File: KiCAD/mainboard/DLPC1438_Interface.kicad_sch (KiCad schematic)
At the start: 92 parts, among them IC14 SN74AUP1G06DCKR, IC6 SN74AUP1G06DCKR, J10 Conn_01x05_Pin, J2 Conn_01x07_Pin, J29 Conn_01x04_Pin, J3 Conn_02x05_Odd_Even, J31 Conn_01x08_Pin, J4 Conn_01x05_Pin, U12 ECS-2520MV-xxx-xx, U13 MX25L3233FM2, U16 DLPC1438ZEZ, U22 TXS0102DCU, U37 TXS0102DCU, U7 SN74AUP1G06DCKR

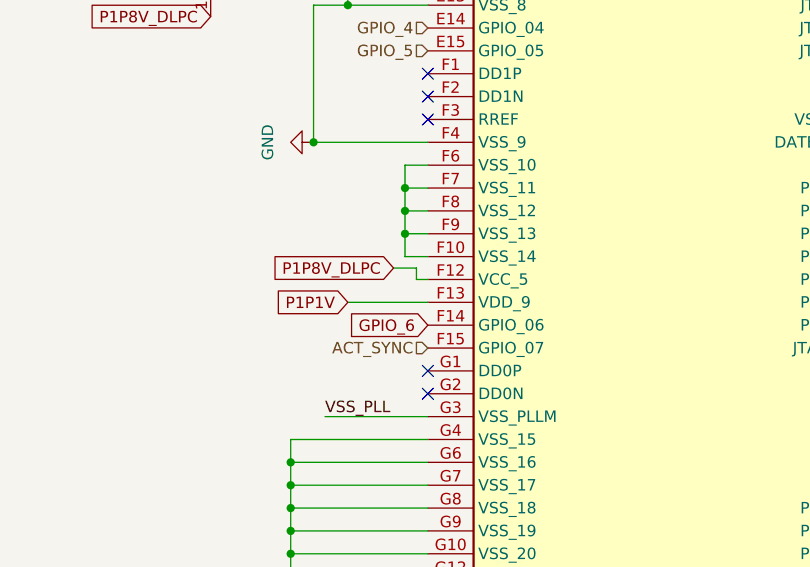
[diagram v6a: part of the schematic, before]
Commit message: layout, was able to fanout all not power signals without vias inside BGA, will only need normal vias size 0.3mm diameter for GND and power planes, plan is to have DMD signals on their own layer
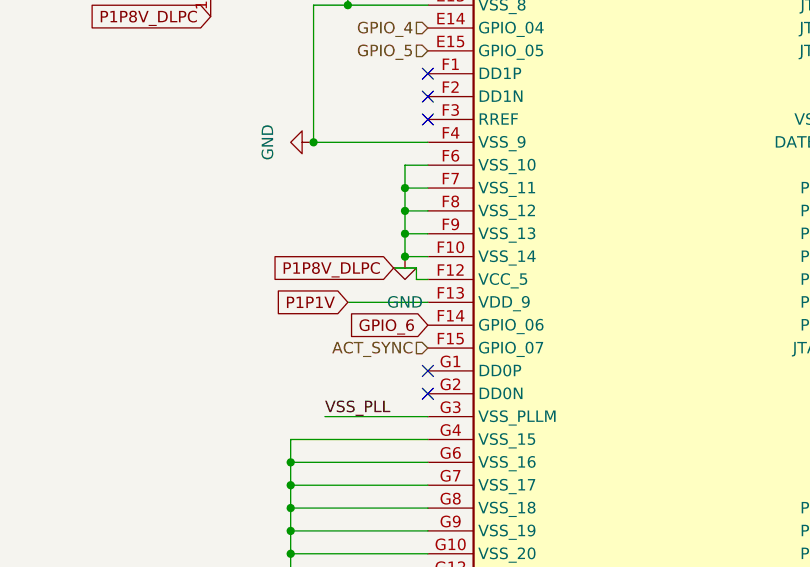
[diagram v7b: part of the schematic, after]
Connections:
- net GND: now also U16.F10 (VSS_14), U16.F6 (VSS_10), U16.F7 (VSS_11), U16.F8 (VSS_12), U16.F9 (VSS_13)
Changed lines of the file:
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@@
 	)
 	(junction
+		(at 359.41 237.49)
+		(diameter 0)
+		(color 0 0 0 0)
+	)
+	(junction
 		(at 251.46 66.04)
 		(diameter 0)
@@
 					(unit 1)
 				)
+			)
+		)
+	)
+	(symbol
+		(lib_id "power:GND")
+		(at 359.41 237.49 0)
+		(unit 1)
+		(exclude_from_sim no)
+		(in_bom yes)
+		(on_board yes)
+		(dnp no)
+		(fields_autoplaced yes)
+		(property "Reference" "#PWR066"
+			(at 359.41 243.84 0)
+			(effects
+				(font
+					(size 1.27 1.27)
+				)
+				(hide yes)
+			)
+		)
+		(property "Value" "GND"
+			(at 359.41 242.57 0)
+			(effects
+				(font
+					(size 1.27 1.27)
+				)
+			)
+		)
+		(property "Footprint" ""
+			(at 359.41 237.49 0)
+			(effects
+				(font
+					(size 1.27 1.27)
+				)
+				(hide yes)
+			)
+		)
+		(property "Datasheet" ""
+			(at 359.41 237.49 0)
+			(effects
+				(font
+					(size 1.27 1.27)
+				)
+				(hide yes)
+			)
+		)
+		(property "Description" "Power symbol creates a global label with name \"GND\" , ground"
+			(at 359.41 237.49 0)
+			(effects
+				(font
+					(size 1.27 1.27)
+				)
+				(hide yes)
+			)
+		)
+		(pin "1"
+		)
+		(instances
+			(project "mainboard"
+				(path "/38e83f42-2cf9-4799-a46f-ca415d95b90a/a69a407c-1a7c-4ac9-a9eb-cd67809c5ec0"
+					(reference "#PWR066")
+					(unit 1)
+				)

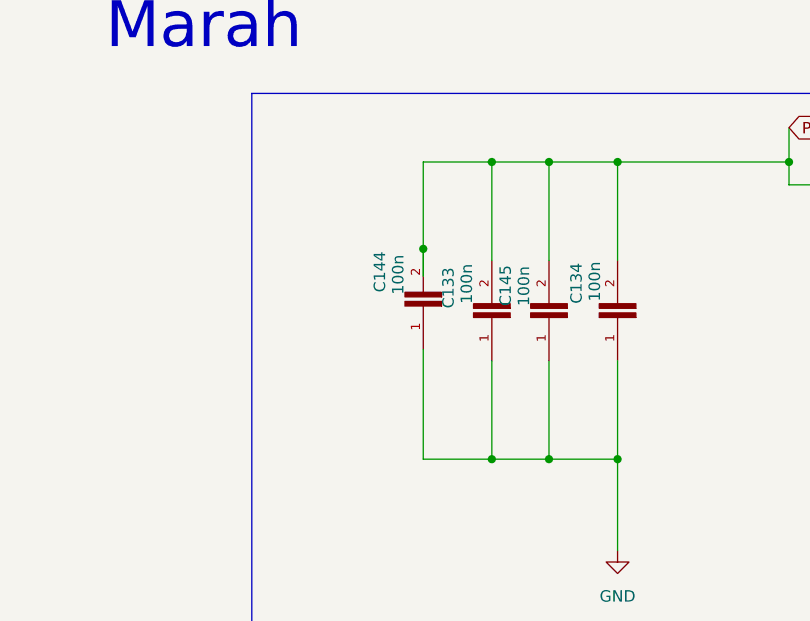
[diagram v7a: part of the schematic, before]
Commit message: added pours to pcb and fixed DLPC capacitor errors
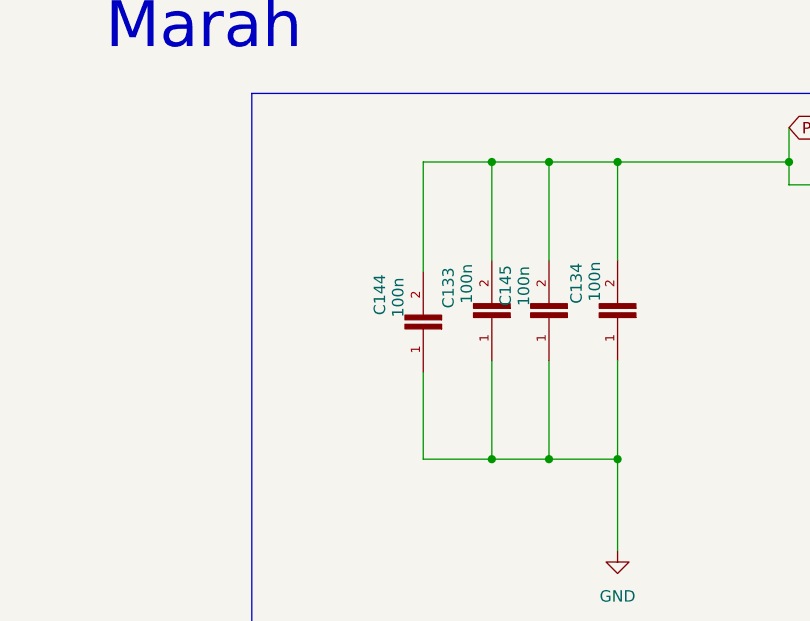
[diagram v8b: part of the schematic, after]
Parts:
- C108, C112, C114, C115, C120, C121, C125, C126, C127, C128, C129, C130, C131, C132, C133, C134, C138, C139, C140, C141, C142, C143, C144, C145, C155, C156, C157, C170, C171, C238, C239, C7: footprint CC0805KRX7R9BB104:CAPC2012X70 -> CAPC2012X70
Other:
- moved on the sheet: C144
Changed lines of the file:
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@@
 	)
 	(junction
-		(at 58.42 50.292)
-		(diameter 0)
-		(color 0 0 0 0)
-	)
-	(junction
 		(at 518.16 143.51)
 		(diameter 0)
@@
 	(wire
 		(pts
-			(xy 58.42 40.64) (xy 58.42 50.292)
-		)
-		(stroke
-			(width 0)
-			(type default)
-		)
-	)
-	(wire
-		(pts
 			(xy 417.83 207.01) (xy 420.37 207.01)
 		)
@@
 	(wire
 		(pts
-			(xy 58.42 50.292) (xy 58.42 53.34)
-		)
-		(stroke
-			(width 0)
-			(type default)
-		)
-	)
-	(wire
-		(pts
 			(xy 433.07 280.67) (xy 433.07 278.13)
 		)
@@
 	(wire
 		(pts
-			(xy 58.42 61.468) (xy 58.42 73.66)
+			(xy 58.42 64.008) (xy 58.42 73.66)
 		)
 		(stroke
@@
 	(wire
 		(pts
+			(xy 58.42 40.64) (xy 58.42 52.832)
+		)
+		(stroke
+			(width 0)
+			(type default)
+		)
+	)
+	(wire
+		(pts
 			(xy 128.27 73.66) (xy 135.89 73.66)
 		)
@@
 			)
 		)
-		(property "Footprint" "CC0805KRX7R9BB104:CAPC2012X70"
+		(property "Footprint" "CAPC2012X70"
 			(at 513.08 226.06 0)
 			(effects
@@
 			)
 		)
-		(property "Footprint" "CC0805KRX7R9BB104:CAPC2012X70"
+		(property "Footprint" "CAPC2012X70"
 			(at 251.46 58.42 0)
 			(effects
@@
 			)
 		)
-		(property "Footprint" "CC0805KRX7R9BB104:CAPC2012X70"
+		(property "Footprint" "CAPC2012X70"
 			(at 114.3 228.6 0)
 			(effects
@@
 			)
 		)
-		(property "Footprint" "CC0805KRX7R9BB104:CAPC2012X70"
+		(property "Footprint" "CAPC2012X70"
 			(at 186.69 58.42 0)
 			(effects
@@
 			)
 		)
-		(property "Footprint" "CC0805KRX7R9BB104:CAPC2012X70"
+		(property "Footprint" "CAPC2012X70"
 			(at 260.35 58.42 0)
 			(effects
@@
 			)
 		)
-		(property "Footprint" "CC0805KRX7R9BB104:CAPC2012X70"
+		(property "Footprint" "CAPC2012X70"
 			(at 123.19 133.35 0)
 			(effects
@@
 			)
 		)
-		(property "Footprint" "CC0805KRX7R9BB104:CAPC2012X70"
+		(property "Footprint" "CAPC2012X70"
 			(at 252.73 134.62 0)
 			(effects
@@
 	(symbol
 		(lib_id "CC0805KRX7R9BB104:CC0805KRX7R9BB104")
-		(at 58.42 55.88 90)
+		(at 58.42 58.42 90)
 		(unit 1)
 		(exclude_from_sim no)
@@
 		(dnp no)
 		(property "Reference" "C144"
-			(at 53.594 55.118 0)
+			(at 53.594 57.658 0)
 			(effects
 				(font
@@
 		)
 		(property "Value" "100n"
-			(at 55.626 55.372 0)
+			(at 55.626 57.912 0)
 			(effects
 				(font
@@
 			)
 		)
-		(property "Footprint" "CC0805KRX7R9BB104:CAPC2012X70"
-			(at 58.42 55.88 0)
+		(property "Footprint" "CAPC2012X70"
+			(at 58.42 58.42 0)
 			(effects
 				(font
@@
 		)
 		(property "Datasheet" "TMK105BJ104KV-F"
-			(at 58.42 55.88 0)
+			(at 58.42 58.42 0)
 			(effects
 				(font
@@
 		)
 		(property "Description" "Unpolarized capacitor"
-			(at 58.42 55.88 0)
+			(at 58.42 58.42 0)
 			(effects
 				(font
@@
 		)
 		(property "Manufacturer_Part_Number" "CL05B104KO5NNNC"
-			(at 58.42 55.88 0)
+			(at 58.42 58.42 0)
 			(effects
 				(font
@@
 		)
 		(property "DigiKey_Part_Number" "311-1140-1-ND"
-			(at 58.42 55.88 0)
+			(at 58.42 58.42 0)
 			(effects
 				(font
@@
 		)
 		(property "SnapEDA_Link" "https://www.snapeda.com/parts/CC0805KRX7R9BB104/Yageo/view-part/?ref=snap"
-			(at 58.42 55.88 0)
+			(at 58.42 58.42 0)
 			(effects
 				(font
@@
 		)
 		(property "Description_1" "0.1 µF ±10% 50V Ceramic Capacitor X7R 0805 (2012 Metric)"
-			(at 58.42 55.88 0)
+			(at 58.42 58.42 0)
 			(effects
 				(font
@@
 		)
 		(property "Package" "0805 Yageo"
-			(at 58.42 55.88 0)
+			(at 58.42 58.42 0)
 			(effects
 				(font
@@
 		)
 		(property "Check_prices" "https://www.snapeda.com/parts/CC0805KRX7R9BB104/Yageo/view-part/?ref=eda"
-			(at 58.42 55.88 0)
+			(at 58.42 58.42 0)
 			(effects
 				(font
@@
 		)
 		(property "MF" "Yageo"
-			(at 58.42 55.88 0)
+			(at 58.42 58.42 0)
 			(effects
 				(font
@@
 		)
 		(property "MP" "CC0805KRX7R9BB104"
-			(at 58.42 55.88 0)
+			(at 58.42 58.42 0)
 			(effects
 				(font
@@
 		)
 		(property "MANUFACTURER" "YAGEO"
-			(at 58.42 55.88 0)
+			(at 58.42 58.42 0)
 			(effects
 				(font
@@
 			)
 		)
-		(property "Footprint" "CC0805KRX7R9BB104:CAPC2012X70"
+		(property "Footprint" "CAPC2012X70"
 			(at 318.77 132.08 0)
 			(effects
@@
 			)
 		)
-		(property "Footprint" "CC0805KRX7R9BB104:CAPC2012X70"
+		(property "Footprint" "CAPC2012X70"
 			(at 270.51 58.42 0)
 			(effects
@@
 			)
 		)
-		(property "Footprint" "CC0805KRX7R9BB104:CAPC2012X70"
+		(property "Footprint" "CAPC2012X70"
 			(at 242.57 224.79 0)
 			(effects
@@
 			)
 		)
-		(property "Footprint" "CC0805KRX7R9BB104:CAPC2012X70"
+		(property "Footprint" "CAPC2012X70"
 			(at 483.87 180.34 0)
 			(effects
@@
 			)
 		)
-		(property "Footprint" "CC0805KRX7R9BB104:CAPC2012X70"
+		(property "Footprint" "CAPC2012X70"
 			(at 120.65 59.69 0)
 			(effects
@@
 			)
 		)
-		(property "Footprint" "CC0805KRX7R9BB104:CAPC2012X70"
+		(property "Footprint" "CAPC2012X70"
 			(at 72.39 57.15 0)
 			(effects
@@
 			)
 		)
-		(property "Footprint" "CC0805KRX7R9BB104:CAPC2012X70"
+		(property "Footprint" "CAPC2012X70"
 			(at 219.71 58.42 0)
 			(effects
@@
 			)
 		)
-		(property "Footprint" "CC0805KRX7R9BB104:CAPC2012X70"
+		(property "Footprint" "CAPC2012X70"
 			(at 135.89 59.69 0)
 			(effects
@@
 			)
 		)
-		(property "Footprint" "CC0805KRX7R9BB104:CAPC2012X70"
+		(property "Footprint" "CAPC2012X70"
 			(at 210.82 58.42 0)
 			(effects
@@
 			)
 		)
-		(property "Footprint" "CC0805KRX7R9BB104:CAPC2012X70"
+		(property "Footprint" "CAPC2012X70"
 			(at 201.93 58.42 0)
 			(effects
@@
 			)
 		)
-		(property "Footprint" "CC0805KRX7R9BB104:CAPC2012X70"
+		(property "Footprint" "CAPC2012X70"
 			(at 194.31 58.42 0)
 			(effects
@@
 			)
 		)
-		(property "Footprint" "CC0805KRX7R9BB104:CAPC2012X70"
+		(property "Footprint" "CAPC2012X70"
 			(at 66.04 57.15 0)
 			(effects
@@
 			)
 		)
-		(property "Footprint" "CC0805KRX7R9BB104:CAPC2012X70"
+		(property "Footprint" "CAPC2012X70"
 			(at 242.57 134.62 0)
 			(effects
@@
 			)
 		)
-		(property "Footprint" "CC0805KRX7R9BB104:CAPC2012X70"
+		(property "Footprint" "CAPC2012X70"
 			(at 146.05 309.88 0)
 			(effects
@@
 			)
 		)
-		(property "Footprint" "CC0805KRX7R9BB104:CAPC2012X70"
+		(property "Footprint" "CAPC2012X70"
 			(at 95.25 309.88 0)
 			(effects
@@
 			)
 		)
-		(property "Footprint" "CC0805KRX7R9BB104:CAPC2012X70"
+		(property "Footprint" "CAPC2012X70"
 			(at 549.91 139.7 0)
 			(effects
@@
 			)
 		)
-		(property "Footprint" "CC0805KRX7R9BB104:CAPC2012X70"
+		(property "Footprint" "CAPC2012X70"
 			(at 245.11 58.42 0)
 			(effects
@@
 			)
 		)
-		(property "Footprint" "CC0805KRX7R9BB104:CAPC2012X70"
+		(property "Footprint" "CAPC2012X70"
 			(at 142.24 59.69 0)
 			(effects
@@
 			)
 		)
-		(property "Footprint" "CC0805KRX7R9BB104:CAPC2012X70"
+		(property "Footprint" "CAPC2012X70"
 			(at 307.34 181.61 0)
 			(effects
@@
 			)
 		)
-		(property "Footprint" "CC0805KRX7R9BB104:CAPC2012X70"
+		(property "Footprint" "CAPC2012X70"
 			(at 236.22 58.42 0)
 			(effects
@@
 			)
 		)
-		(property "Footprint" "CC0805KRX7R9BB104:CAPC2012X70"
+		(property "Footprint" "CAPC2012X70"
 			(at 227.33 58.42 0)
 			(effects
@@
 			)
 		)
-		(property "Footprint" "CC0805KRX7R9BB104:CAPC2012X70"
+		(property "Footprint" "CAPC2012X70"
 			(at 563.88 147.32 0)
 			(effects
@@
 			)
 		)
-		(property "Footprint" "CC0805KRX7R9BB104:CAPC2012X70"
+		(property "Footprint" "CAPC2012X70"
 			(at 80.01 57.15 0)
 			(effects
@@
 			)
 		)
-		(property "Footprint" "CC0805KRX7R9BB104:CAPC2012X70"
+		(property "Footprint" "CAPC2012X70"
 			(at 128.27 59.69 0)
 			(effects
